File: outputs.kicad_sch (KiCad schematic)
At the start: 27 parts, among them J10 DOUT_5-9, J8 Conn_01x05, J9 DOUT_0-4, U10 ULN2004, U9 ULN2004

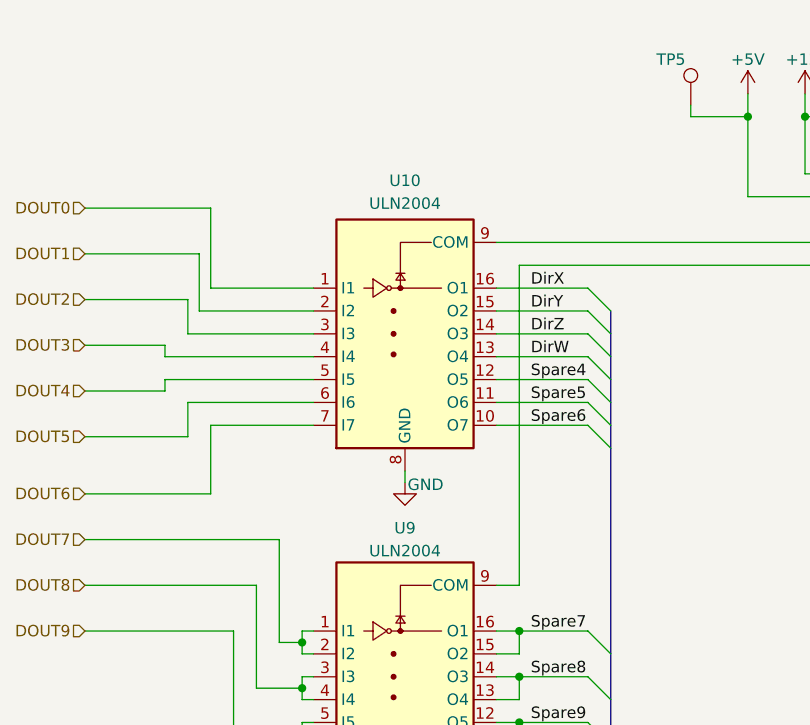
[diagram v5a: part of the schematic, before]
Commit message: Se reemplaza ULN2004 por ULN2003 ya que este último es compatible con entradas 3V3. Se optimiza el pcb en cuanto a pistas y planos de masa debajo de los ULN.
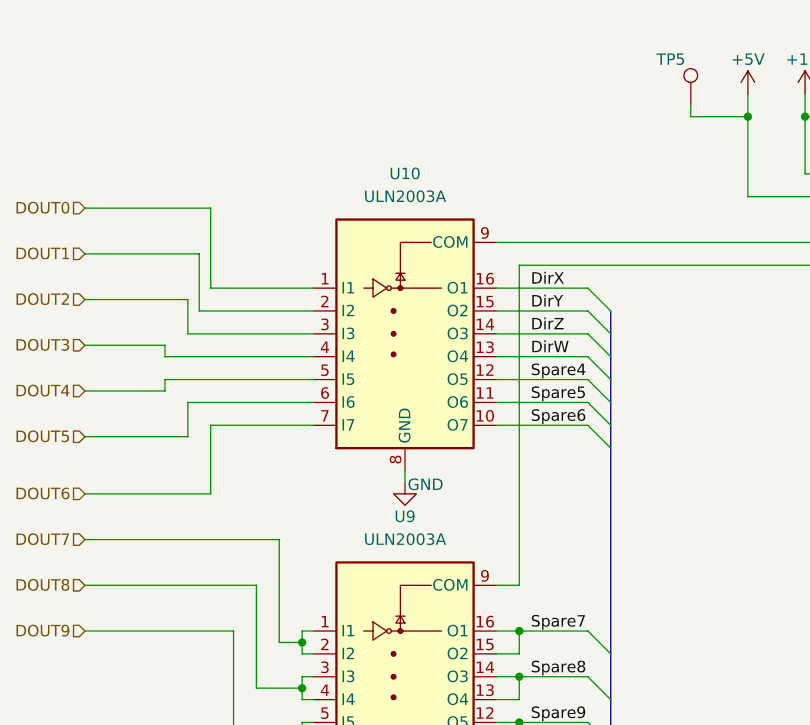
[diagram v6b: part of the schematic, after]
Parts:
- U10, U9: value ULN2004 -> ULN2003A
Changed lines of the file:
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@@
 		(fields_autoplaced yes)
 		(property "Reference" "U10"
-			(at 68.58 104.902 0)
-			(effects
-				(font
-					(size 1.27 1.27)
-				)
-			)
-		)
-		(property "Value" "ULN2004"
-			(at 68.58 107.442 0)
+			(at 68.58 104.14 0)
+			(effects
+				(font
+					(size 1.27 1.27)
+				)
+			)
+		)
+		(property "Value" "ULN2003A"
+			(at 68.58 106.68 0)
 			(effects
 				(font
@@
 		(fields_autoplaced yes)
 		(property "Reference" "U9"
-			(at 68.58 143.51 0)
-			(effects
-				(font
-					(size 1.27 1.27)
-				)
-			)
-		)
-		(property "Value" "ULN2004"
-			(at 68.58 146.05 0)
-			(effects
-				(font
+			(at 68.58 142.24 0)
+			(effects
+				(font
+					(size 1.27 1.27)
+				)
+			)
+		)
+		(property "Value" "ULN2003A"
+			(at 68.58 144.78 0)
+			(effects
+				(font
